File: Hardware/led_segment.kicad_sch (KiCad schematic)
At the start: 28 parts

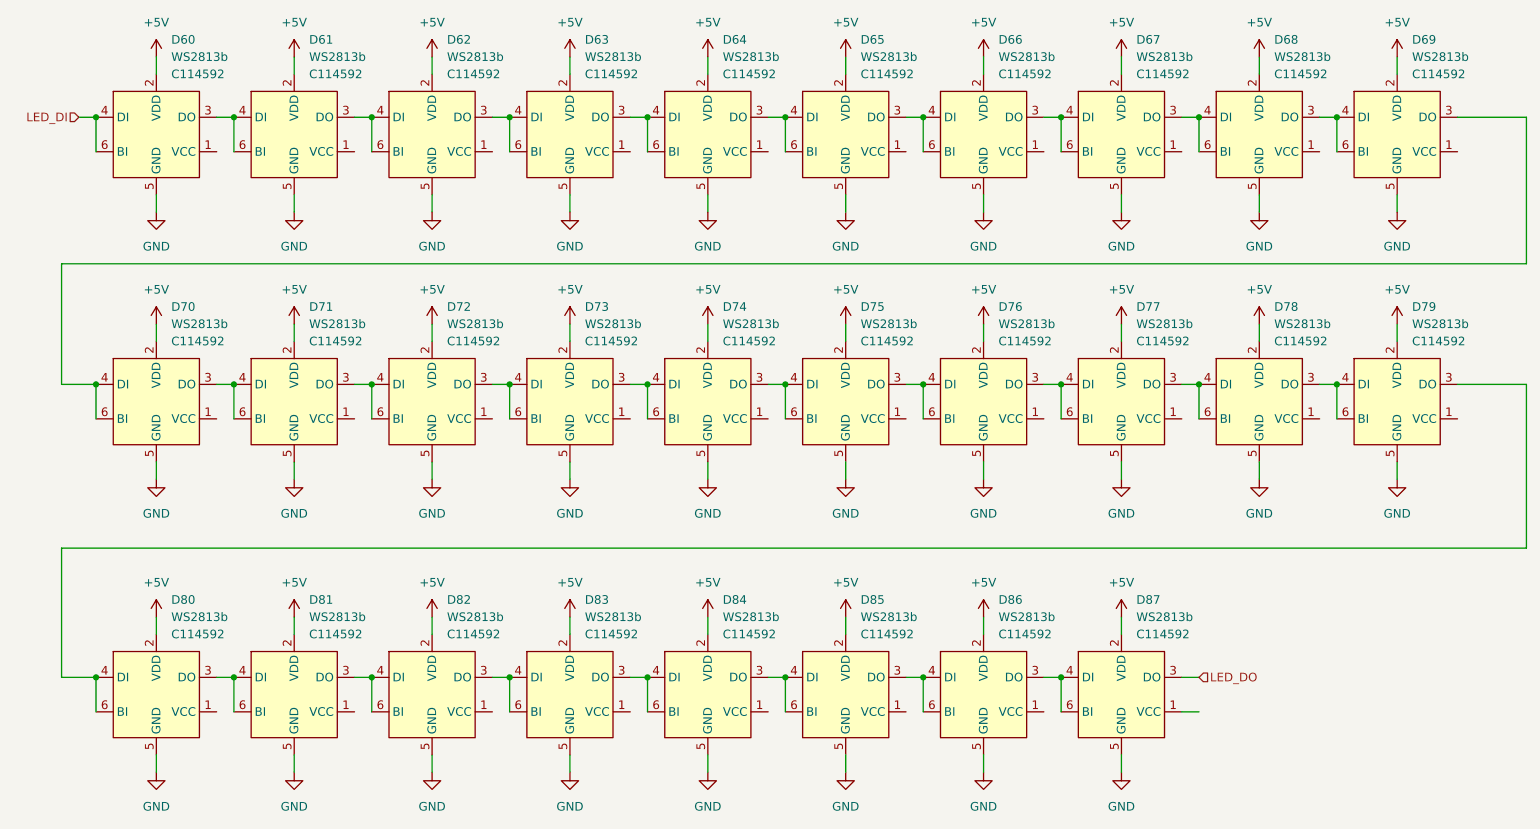
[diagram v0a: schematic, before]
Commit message: Added ESP32-WROOM
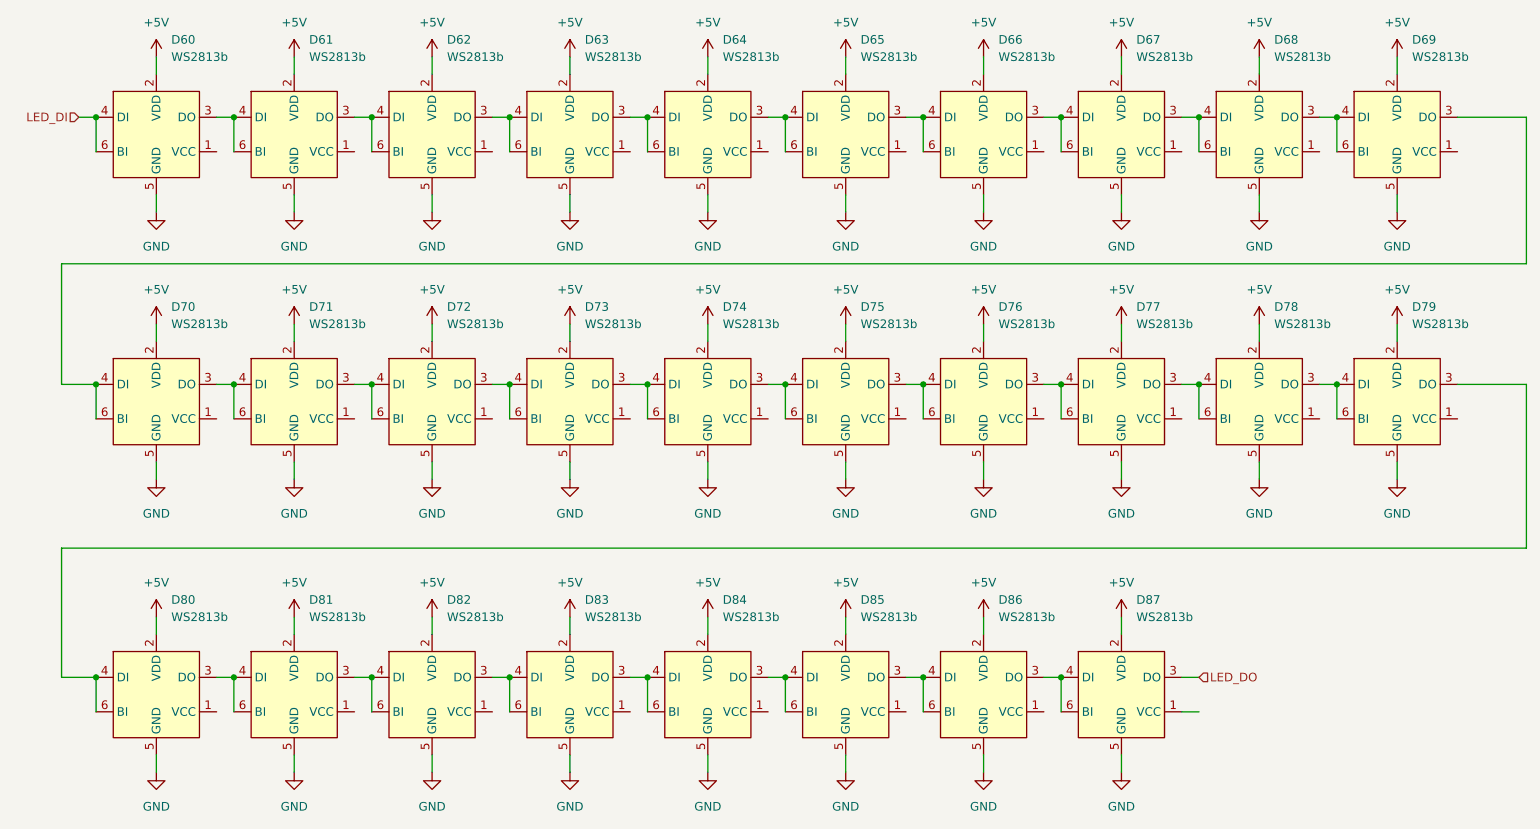
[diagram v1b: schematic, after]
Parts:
- D60, D61, D62, D63, D64, D65, D66, D67, D68, D69, D70, D71, D72, D73, D74, D75, D76, D77, D78, D79, D80, D81, D82, D83, D84, D85, D86, D87: LCSC C114592 -> (none); lcsc_new C114592 -> (none)
